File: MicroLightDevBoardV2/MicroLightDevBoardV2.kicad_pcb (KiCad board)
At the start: 2 copper layers, 86.2 x 76.5 mm, 83 parts, among them J1 Conn_01x02_Socket, J10 Conn_01x02_Socket, J11 Conn_01x02_Socket, J12 TYPE-C-31-M-12, J13 Conn_01x02_Socket, J14 Conn_01x02_Socket, J15 Conn_01x02_Socket, J16 Conn_01x04_Socket, J17 Conn_01x02_Socket, J18 Conn_01x02_Socket, J19 Conn_01x04_Socket, J2 Conn_01x02_Socket, J20 Conn_01x04_Socket, J21 Conn_01x02_Socket, J22 Conn_01x02_Socket, J23 Conn_01x02_Socket, J24 Conn_01x02_Socket, J25 Conn_01x02_Socket, J26 Conn_01x04_Socket, J27 Conn_01x02_Socket, J28 Conn_01x04_Socket, J29 Conn_01x04_Socket, J3 Conn_01x04_Socket, J30 Conn_01x04_Socket, J31 Conn_01x04_Socket, J32 Conn_01x04_Socket, J33 Conn_01x04_Socket, J34 Conn_01x04_Socket, J35 Conn_01x04_Socket, J36 Conn_01x04_Socket, J37 Conn_01x04_Socket, J38 Conn_01x04_Socket, J39 Conn_01x04_Socket, J4 Conn_01x04_Socket, J40 Conn_01x04_Socket, J41 Conn_01x04_Socket, J42 Conn_01x04_Socket, J43 Conn_01x04_Socket, J44 Conn_01x04_Socket, J45 Conn_01x04_Socket, J46 Conn_01x04_Socket, J47 Conn_01x04_Socket, J48 Conn_01x04_Socket, J49 Conn_01x04_Socket, J5 Conn_01x05_Socket, J50 Conn_01x04_Socket, J6 Conn_01x05_Socket, J7 Conn_01x05_Socket, J8 Conn_01x05_Socket, J9 Conn_01x02_Socket, U1 BQ25180, U2 ATtiny3226-M, U3 S-85S1AB33-I6T1U, U4 B3U-1000P, U5 B3U-1000P, U6 USBLC6-2P6, U7 MC3479

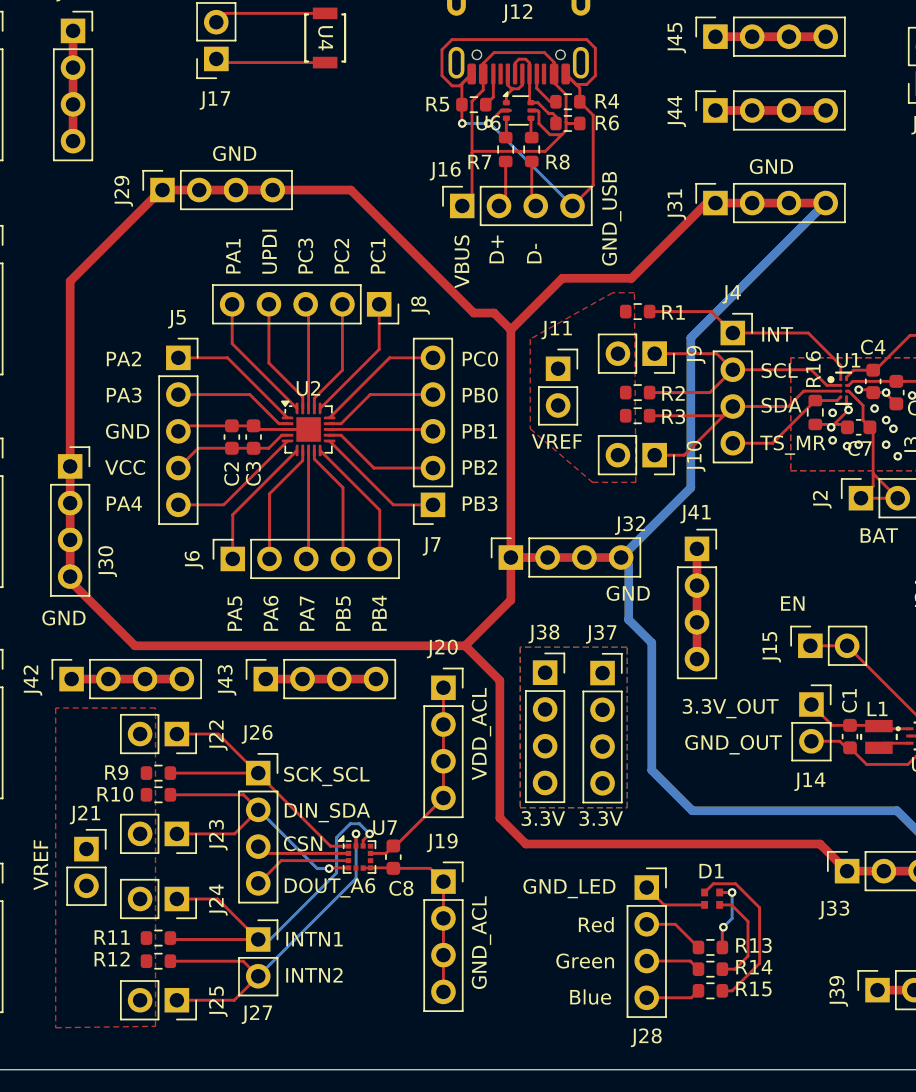
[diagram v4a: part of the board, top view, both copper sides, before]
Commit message: add lcsc part numbers
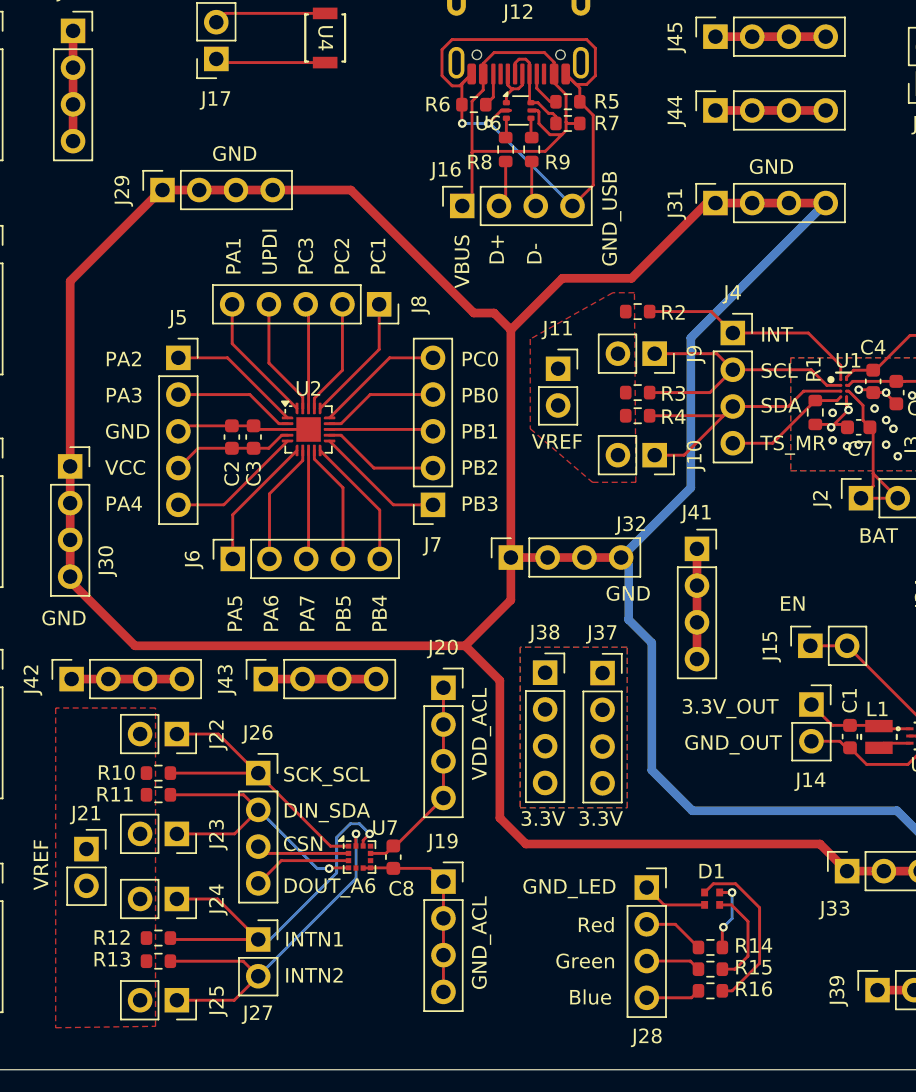
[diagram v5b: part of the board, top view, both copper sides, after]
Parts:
- C2: value 10 nF -> 10nF
- C3: value 100 nF -> 100nF
- C4, C7: value 1uh 25v -> 1uF 25v
- C5: value 10uh -> 10uF
- C8: value 0.1uf -> 100nF
- renumbered R16 to R1, R9 to R10, R10 to R11, R11 to R12, R12 to R13, R13 to R14, R14 to R15, R15 to R16, R1 to R2, R2 to R3, R3 to R4, R4 to R5, R5 to R6, R6 to R7, R7 to R8, R8 to R9

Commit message: changed inductor so jlcpcb doesn't try to autofill some random one
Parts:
- L1: value 2.2uH -> 74438343022 2.2uH

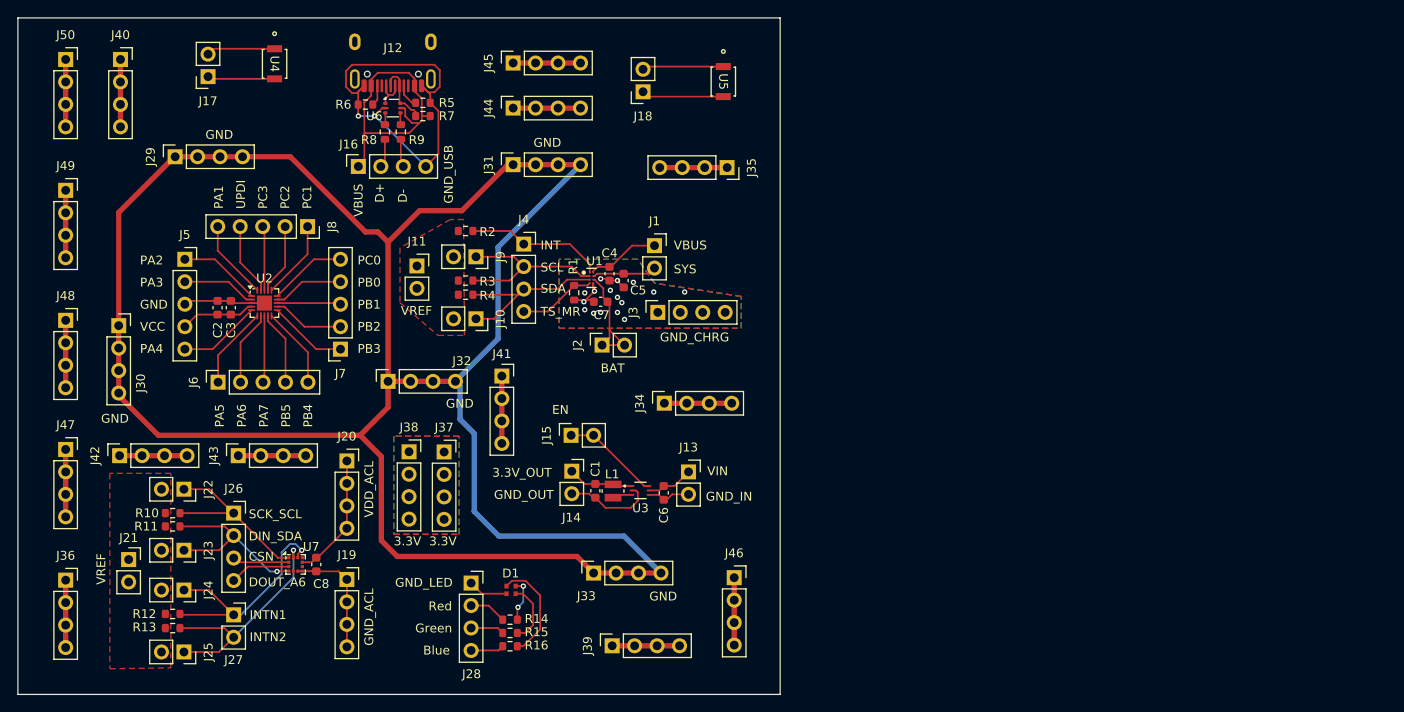
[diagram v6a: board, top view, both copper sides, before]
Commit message: updated led resistor values for 3.3v
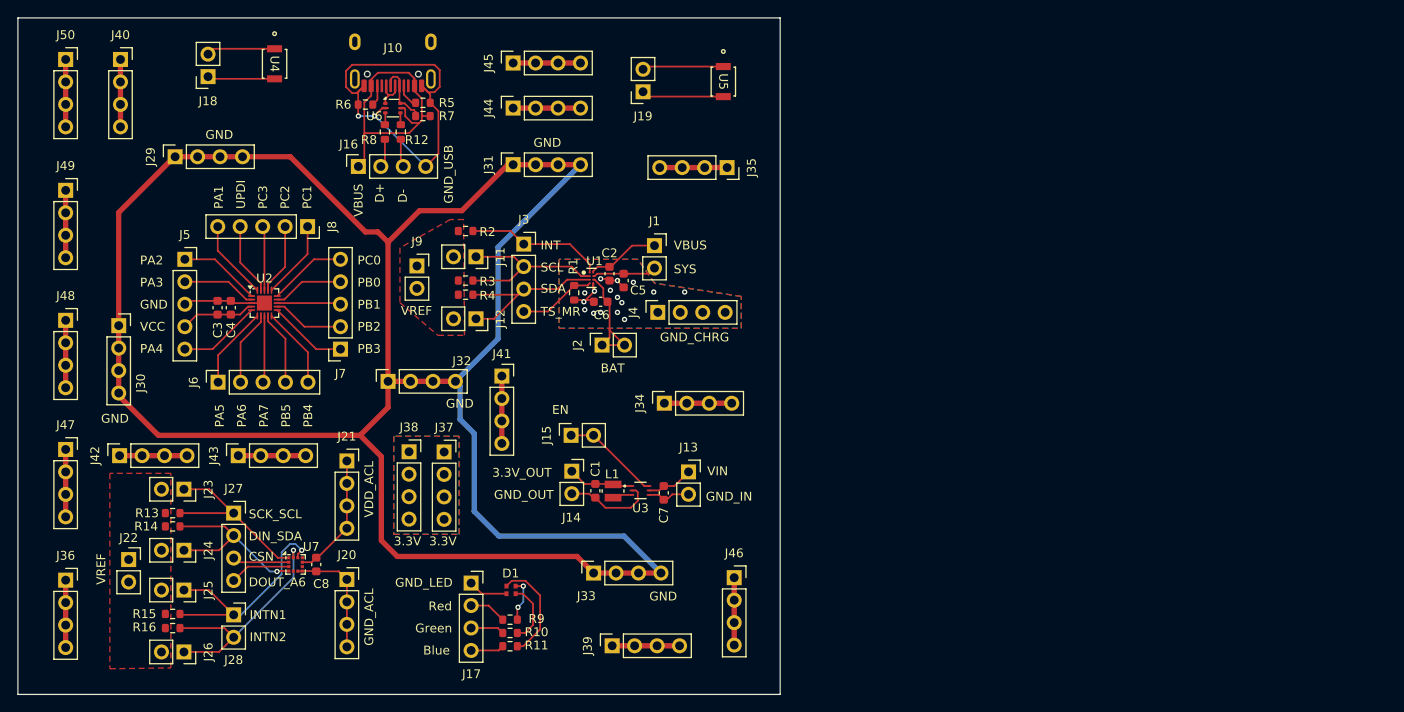
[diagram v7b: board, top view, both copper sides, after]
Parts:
- R10: renamed from R15; value 47 -> 30
- R11: renamed from R16; value 56 -> 30
- R9: renamed from R14; value 68 -> 51
- renumbered C4 to C2, C2 to C3, C3 to C4, C7 to C6, C6 to C7, J12 to J10, J9 to J11, J10 to J12, J28 to J17, J17 to J18, J18 to J19, J19 to J20, J20 to J21, J21 to J22, J22 to J23, J23 to J24, J24 to J25, J25 to J26, J26 to J27, J27 to J28, J4 to J3, J3 to J4, J11 to J9, R9 to R12, R10 to R13, R11 to R14, R12 to R15, R13 to R16
